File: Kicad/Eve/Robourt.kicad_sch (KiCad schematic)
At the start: 5 parts, among them J9 Conn_ST_STDC14

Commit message: Kicad changes
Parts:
- added C3, C5, C6, C7: 100n, Capacitor_SMD:C_0603_1608Metric_Pad1.08x0.95mm_HandSolder, symbol Device:C
- added C4: 4.7u, Capacitor_SMD:C_0603_1608Metric_Pad1.08x0.95mm_HandSolder, symbol Device:C
- added D2 (x2), D3, D4, D5, D6: LED, LED_SMD:LED_0603_1608Metric_Pad1.05x0.95mm_HandSolder, symbol Device:LED
- added IC1: STM32U535RET6, QFP50P1200X1200X160-64N, symbol STM32U535RET6:STM32U535RET6
- added J2: Conn_01x02, Connector_JST:JST_XH_B2B-XH-A_1x02_P2.50mm_Vertical, symbol Connector_Generic:Conn_01x02
- added J6: Conn_02x20_Odd_Even, Connector_PinHeader_2.54mm:PinHeader_2x20_P2.54mm_Vertical, symbol Connector_Generic:Conn_02x20_Odd_Even
- added R2: 100k, Resistor_SMD:R_0603_1608Metric_Pad0.98x0.95mm_HandSolder, symbol Device:R_Small
- added R3, R4, R5, R6, R7: 1k, Resistor_SMD:R_0603_1608Metric_Pad0.98x0.95mm_HandSolder, symbol Device:R_Small
- added R3: 1k, Resistor_SMD:R_0603_1608Metric_Pad0.98x0.95mm_HandSolder, symbol Device:R
- added SW1: SW_Push, Button_Switch_SMD:SW_SPST_B3U-1000P, symbol Switch:SW_Push
- added U2: STM32L412KBT6, Package_QFP:LQFP-32_7x7mm_P0.8mm, symbol MCU_ST_STM32L4:STM32L412KBTx
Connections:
- net +3.3V: now also C4.1, C5.1, C6.1, C7.1, IC1.13 (VDDA), IC1.19 (VDD_1), IC1.32 (VDD_2), IC1.48 (VDDUSB), IC1.64 (VDD_3), U2.1 (VDD), U2.17 (VDD), U2.5 (VDDA)
- net GND: now also C3.1, C4.2, C5.2, C6.2, C7.2, D2.1 (K), D3.1 (K), D4.1 (K), D5.1 (K), D6.1 (K), IC1.12 (VSSA), IC1.18 (VSS_1), IC1.31 (VSS_2), IC1.47 (VSS_3), IC1.63 (VSS_4), J2.1 (Pin_1), R2.1, R3.2, SW1.1, U2.16 (VSS), U2.32 (VSS)
- net NRST: now also C3.2, SW1.2, U2.4 (NRST)
- net SYS_JTMS-SWCLK: now also U2.24 (PA14)
- net SYS_JTMS-SWDIO: now also U2.23 (PA13)
- new net: D2.2 (A), R3.2
- new net: D6.2 (A), R7.2
- new net: D4.2 (A), R5.2
- new net: D2.1 (K), R3.1
- new net: D5.2 (A), R6.2
- new net: D3.2 (A), R4.2
- new net +24V: J2.2 (Pin_2), R3.1
- new net 12V: R4.1
- new net 3.3V: R7.1
- new net 5.1V: R6.1
- new net 7.2V: R5.1
- new net BOOT0: R2.2, U2.31 (PH3)
- new net Dir_1: U2.11 (PA5)
- new net Dir_2: U2.13 (PA7)
- new net Dir_3: U2.15 (PB1)
- new net LPUART1_RX: IC1.8 (PC0)
- new net LPUART1_TX: IC1.9 (PC1)
- new net Servo_TX: U2.8 (PA2)
- new net Setpper_Capt_Pos_1: U2.18 (PA8)
- new net Setpper_Capt_Pos_2: U2.19 (PA9)
- new net Setpper_Capt_Pos_3: U2.20 (PA10)
- new net Step_1: U2.10 (PA4)
- new net Step_2: U2.12 (PA6)
- new net Step_3: U2.14 (PB0)
- new net Test_LED: D2.2 (A), U2.9 (PA3)
- new net UART4_TX: IC1.14 (PA0)
- new net UART5_TX: IC1.53 (PC12)
- new net USART1_RX: U2.30 (PB7)
- new net USART1_TX: IC1.58 (PB6), U2.29 (PB6)
- new net USART3_TX: IC1.23 (PA7)
- no-connect marks 5 -> 15
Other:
- added sheet Régulateur 11.1V (reg3.kicad_sch)
- added sheet Régulateur 3.3V (untitled.kicad_sch)
- added sheet Régulateur 5.1V (Reg2.kicad_sch)
- added sheet Régulateur 7.4V (reg4.kicad_sch)
- sheet driver_stepper ports: added CLK, CON_DIR, CON_STEP, CSN, ENN, EXT_DIR, EXT_STEP, GND, MISO, MOSI, SCK, SG_TST, STANDALONE_MODE, VCC_IO, Vdc; removed C_Moins, C_Plus
- sheet driver_stepper1 ports: added none; removed C_Moins, C_Plus
- sheet driver_stepper2 ports: added CLK, CON_DIR, CON_STEP, CSN, ENN, EXT_DIR, EXT_STEP, GND, MISO, MOSI, SCK, SG_TST, STANDALONE_MODE, VCC_IO, Vdc; removed C_Moins, C_Plus
- note added: "1* 100nF per VDD pin"
- note added: "Connecteurs Stepper"
- note removed: "Connecteurs moteurs"
- note removed: "Power input"
- title: Projet Robourt -> Projet EVE
- moved on the sheet: H1, H2, H3, H4, J9

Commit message: updtated Kicad ver 7.11.23
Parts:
- removed D3, D4, D5, D6: LED, LED_SMD:LED_0603_1608Metric_Pad1.05x0.95mm_HandSolder, symbol Device:LED
- removed R2: 100k, Resistor_SMD:R_0603_1608Metric_Pad0.98x0.95mm_HandSolder, symbol Device:R_Small
- removed R4, R5, R6, R7: 1k, Resistor_SMD:R_0603_1608Metric_Pad0.98x0.95mm_HandSolder, symbol Device:R_Small
- removed U2: STM32L412KBT6, Package_QFP:LQFP-32_7x7mm_P0.8mm, symbol MCU_ST_STM32L4:STM32L412KBTx
- added J4, J5: Conn_01x03, symbol Connector_Generic:Conn_01x03
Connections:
- net GND: now also J4.3 (Pin_3), J5.3 (Pin_3)
- net NRST: now also IC1.7 (NRST)
- net SYS_JTMS-SWCLK: now also IC1.49 (PA14)
- net SYS_JTMS-SWDIO: now also IC1.46 (PA13)
- net Test_LED: now also IC1.15 (PA1)
- net USART1_TX: now also J5.1 (Pin_1)
- net USART3_TX: now also J4.1 (Pin_1)
- net SPI2_MISO: now reaches IC1.10 (PC2)
- net SPI2_MOSI: now reaches IC1.11 (PC3)
- net CLK: now reaches IC1.16 (PA2)
- net SCK: now reaches IC1.29 (PB10)
- net GPIO_DIR3: now reaches IC1.37 (PC6)
- net GPIO_STEP3: now reaches IC1.38 (PC7)
- net GPIO_DIR2: now reaches IC1.39 (PC8)
- net GPIO_STEP2: now reaches IC1.40 (PC9)
- net GPIO_DIR1: now reaches IC1.41 (PA8)
- net GPIO_STEP1: now reaches IC1.42 (PA9)
- net GPIO_CSN3: now reaches IC1.43 (PA10)
- net GPIO_CSN2: now reaches IC1.44 (PA11)
- net GPIO_CSN1: now reaches IC1.45 (PA12)
- new net 11.7V: J5.2 (Pin_2)
- new net 7.5V: J4.2 (Pin_2)
- no-connect marks 15 -> 85
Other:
- sheet Régulateur 11.1V renamed Régulateur 11.7V
- sheet Régulateur 7.4V renamed Régulateur 7.5V
- sheet Régulateur 11.7V ports: added 11.7V, 24V; removed none
- sheet Régulateur 3.3V ports: added 24V; removed none
- sheet Régulateur 5.1V ports: added 24V; removed none
- sheet Régulateur 7.5V ports: added 24V, 7.5V; removed none
- sheet driver_stepper ports: added DIR, SDI, SDO, STEP; removed CON_DIR, CON_STEP, EXT_DIR, EXT_STEP, GND, MISO, MOSI
- sheet driver_stepper1 ports: added SDI, SDO, Vdc; removed A1, A2, B1, B2, GND, MISO, MOSI
- sheet driver_stepper2 ports: added DIR, SDI, SDO, STEP; removed CON_DIR, CON_STEP, EXT_DIR, EXT_STEP, GND, MISO, MOSI
- note added: "Connecteurs"
- note removed: "Connecteurs Stepper"
- moved on the sheet: D2, IC1, J2, J6, J9, R3

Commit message: KiCad changes 10/11
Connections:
- net 7.5V: no longer J4.2 (Pin_2)
- net UART4_TX: now also J9.13 (VCP_RX)
- net UART4_RX: now reaches IC1.52 (PC11)
- net UART4_RX: now also J9.14 (VCP_TX)
- net CLK: no longer names the net of IC1.16 (PA2)
- new net +7.5V: J4.2 (Pin_2)
- no-connect marks 85 -> 86
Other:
- sheet Régulateur 3.3V ports: added 5.1V; removed 24V
- note added: "XL320"
- note added: "XL430"

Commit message: Kicad changes 11/11/22 added quartz
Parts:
- added C37, C8: 20p, symbol Device:C_Small
- added Y1: ECS-320-6-47B2-CTN-TR, ECS320647B2CTNTR, symbol ECS-320-6-47B2-CTN:ECS-320-6-47B2-CTN-TR
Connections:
- net GND: now also C37.1, C8.2, Y1.2 (GND_1), Y1.4 (GND_2)
- net OSC_in: now reaches IC1.5 (PH0-OSC_IN)
- net OSC_in: now also C37.2, Y1.3 (OUT/IN)
- net OSC_out: now reaches IC1.6 (PH1-OSC_OUT)
- net OSC_out: now also C8.1, Y1.1 (IN/OUT)
- no-connect marks 86 -> 84
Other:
- note added: "Oscillateur Quartz"
- moved on the sheet: C3, C4, C5, C6, C7, D2, H1, H2, H3, H4, IC1, J2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

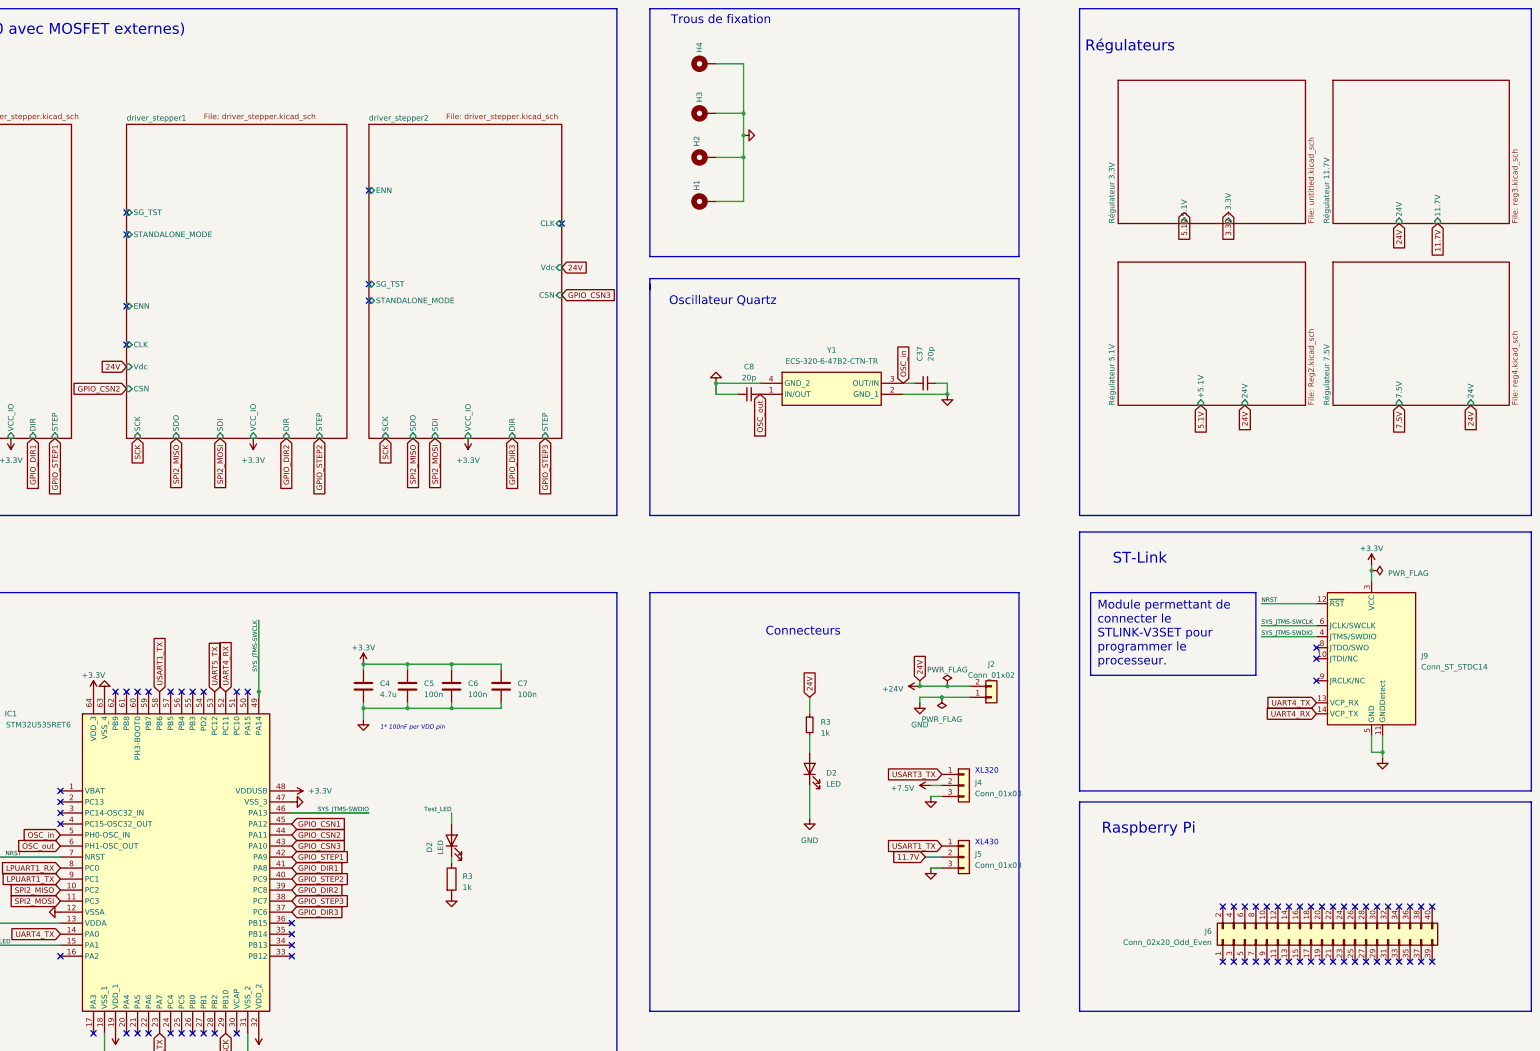
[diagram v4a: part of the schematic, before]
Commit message: added Kicad libraries to git + sch changes 11/11/23
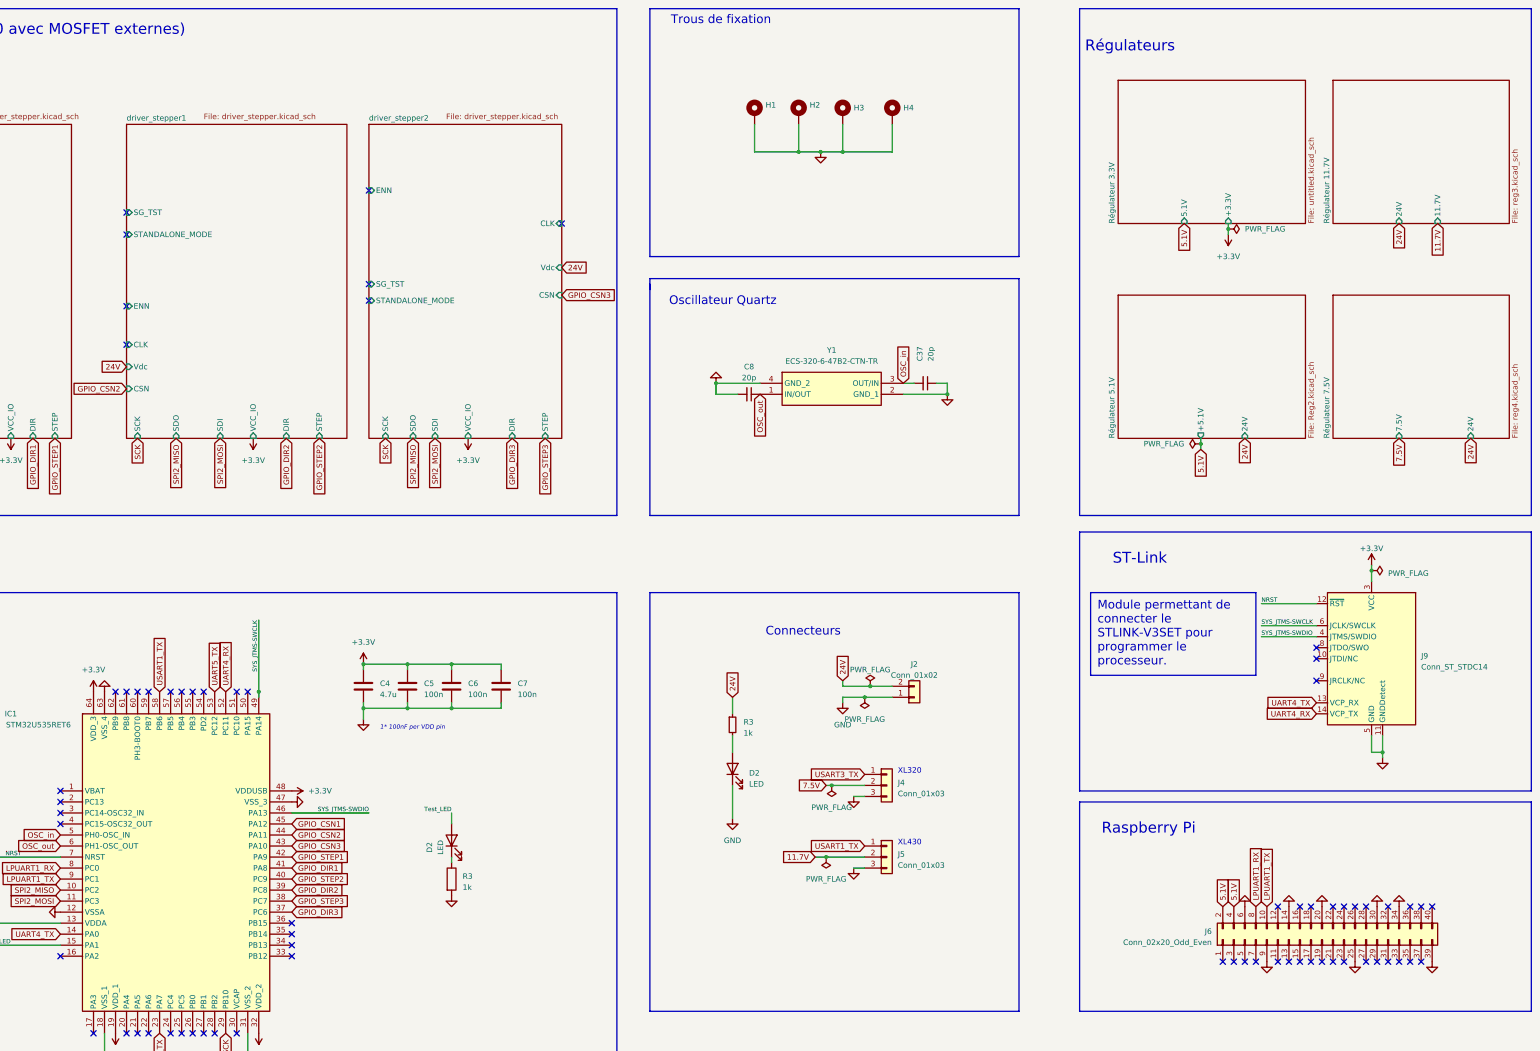
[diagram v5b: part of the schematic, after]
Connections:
- net +7.5V is gone; now on net 7.5V: J4.2 (Pin_2)
- net 5.1V: now also J6.2 (Pin_2), J6.4 (Pin_4)
- net GND: now also J6.14 (Pin_14), J6.20 (Pin_20), J6.25 (Pin_25), J6.30 (Pin_30), J6.34 (Pin_34), J6.39 (Pin_39), J6.6 (Pin_6), J6.9 (Pin_9)
- net LPUART1_RX: now also J6.8 (Pin_8)
- net LPUART1_TX: now also J6.10 (Pin_10)
- net +24V renamed 24V
- no-connect marks 84 -> 72
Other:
- moved on the sheet: D2, H1, H2, H3, H4, J2, J4, J5, R3

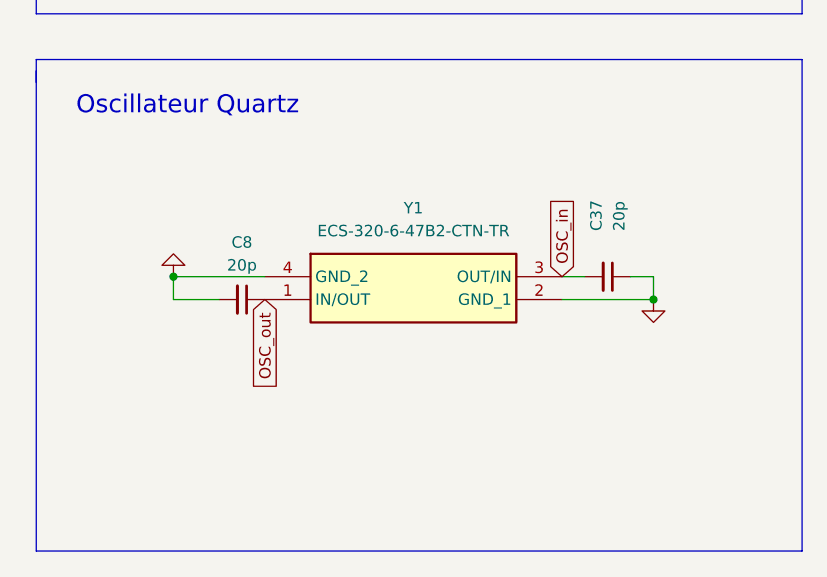
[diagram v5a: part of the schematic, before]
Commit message: changed quartz 12/11/23
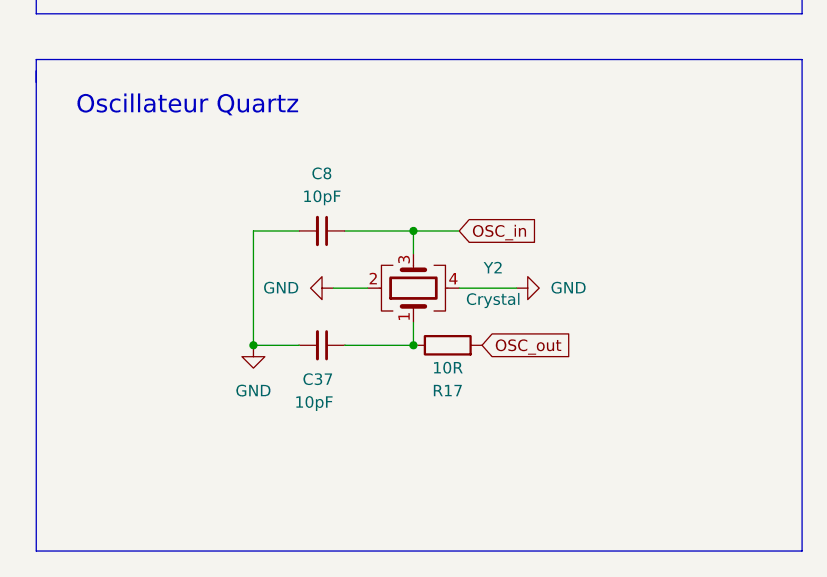
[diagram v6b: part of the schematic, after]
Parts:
- removed Y1: ECS-320-6-47B2-CTN-TR, ECS320647B2CTNTR, symbol ECS-320-6-47B2-CTN:ECS-320-6-47B2-CTN-TR
- added R17: 10R, symbol Device:R
- added Y2: Crystal, Crystal:Crystal_SMD_EuroQuartz_MT-4Pin_3.2x2.5mm, symbol Device:Crystal_GND24
- C37, C8: value 20p -> 10pF
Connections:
- net GND: now also C37.2, Y2.2, Y2.4; no longer C37.1
- net OSC_in: now also C8.1, Y2.3; no longer C37.2
- net OSC_out: now also R17.2; no longer C8.1
- new net: C37.1, R17.1, Y2.1
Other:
- moved on the sheet: C37, C8
